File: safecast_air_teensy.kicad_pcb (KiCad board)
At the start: 2 copper layers, 108 x 69.8 mm, 22 parts, among them P1 CONN_5X2, P2 CONN_5X2, P3 CONN_7X2, P4 CONN_2X2, P5 CONN_2, P6 CONN_2, P7 CONN_2, P8 CONN_3X2, P9 CONN_2, U1 GPS, U2 XBEE, U3 LCD, U4 OPENLOG, U5 POLOLU_3V3, U6 TEENSY3.1, U7 R5_BUSSED

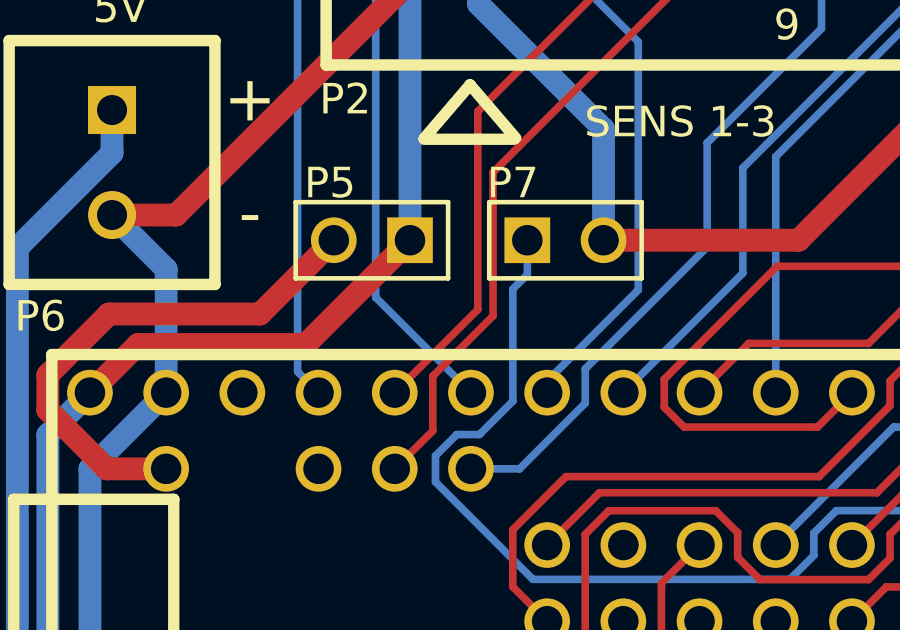
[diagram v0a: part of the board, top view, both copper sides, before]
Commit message: Added missing silkscreen elements (5V VBUS) and PROG.
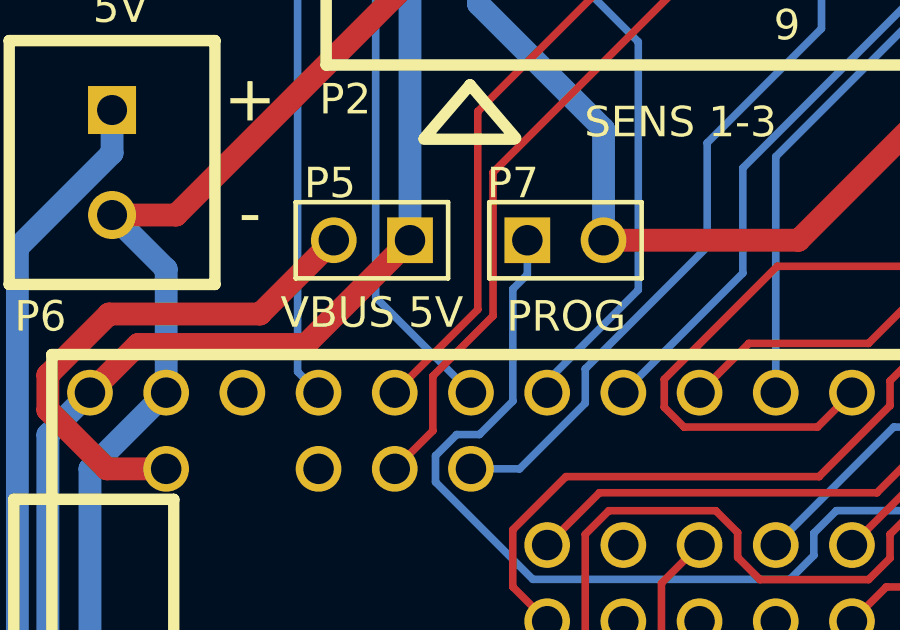
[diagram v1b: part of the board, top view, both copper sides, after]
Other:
- board text added: "PROG"
- board text added: "VBUS 5V"
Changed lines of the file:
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@@
     (area 25.349999 25.349999 133.400001 95.3516)
     (thickness 1.6)
-    (drawings 22)
+    (drawings 24)
     (tracks 409)
     (zones 0)
@@
     (uvia_min_size 0.508)
     (uvia_min_drill 0.127)
-    (pcb_text_width 0.3048)
-    (pcb_text_size 1.524 1.524)
+    (pcb_text_width 0.2032)
+    (pcb_text_size 1.016 1.016)
     (mod_edge_width 0.15)
     (mod_text_size 1 1)
@@
     (visible_elements FFFFFFBF)
     (pcbplotparams
-      (layerselection 3178497)
+      (layerselection 284196865)
       (usegerberextensions true)
       (excludeedgelayer true)
@@
       (outputformat 1)
       (mirror false)
-      (drillshape 1)
+      (drillshape 0)
       (scaleselection 1)
-      (outputdirectory ""))
+      (outputdirectory gerber_v0p1_r1/))
   )
   (net 0 "")
@@
     )
   )
+  (gr_text PROG (at 44.831 44.958) (layer F.SilkS)
+    (effects (font (size 1.016 1.016) (thickness 0.2032)))
+  )
+  (gr_text "VBUS 5V" (at 38.354 44.831) (layer F.SilkS)
+    (effects (font (size 1.016 1.016) (thickness 0.2032)))
+  )
   (gr_text "Safecast Air Prototype V0.1 R1\nwww.iorodeo.com" (at 82.804 61.341 180) (layer B.SilkS)

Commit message: Finished first version of Revision 2.
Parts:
- added R1: R, R_SMALL, F.Cu at (38.0, 41.0)
- added R10: R, R_SMALL, F.Cu at (65.0, 41.0)
- added R11: R, R_SMALL, F.Cu at (68.0, 41.0)
- added R12: R, R_SMALL, F.Cu at (72.0, 38.0)
- added R13: R, R_SMALL, F.Cu at (75.0, 38.0)
- added R14: R, R_SMALL, F.Cu at (78.0, 38.0)
- added R15: R, R_SMALL, F.Cu at (81.0, 38.0)
- added R16: R, R_SMALL, F.Cu at (84.0, 38.0)
- added R17: R, R_SMALL, F.Cu at (87.0, 38.0)
- added R18: R, R_SMALL, F.Cu at (90.0, 38.0)
- added R19: R, R_SMALL, F.Cu at (72.0, 48.0)
- added R2: R, R_SMALL, F.Cu at (41.0, 41.0)
- added R20: R, R_SMALL, F.Cu at (75.0, 48.0)
- added R21: R, R_SMALL, F.Cu at (78.0, 48.0)
- added R22: R, R_SMALL, F.Cu at (81.0, 48.0)
- added R23: R, R_SMALL, F.Cu at (84.0, 48.0)
- added R24: R, R_SMALL, F.Cu at (87.0, 48.0)
- added R3: R, R_SMALL, F.Cu at (44.0, 41.0)
- added R4: R, R_SMALL, F.Cu at (47.0, 41.0)
- added R5: R, R_SMALL, F.Cu at (50.0, 41.0)
- added R6: R, R_SMALL, F.Cu at (53.0, 41.0)
- added R7: R, R_SMALL, F.Cu at (56.0, 41.0)
- added R8: R, R_SMALL, F.Cu at (59.0, 41.0)
- added R9: R, R_SMALL, F.Cu at (62.0, 41.0)
- P1, P2: footprint 5X2_SHRD_HEADER -> 5X2_2MM_SHRD_HEADER
- P3: value CONN_7X2 -> CONN_5X2; footprint 7X2_SHRD_HEADER -> 5X2_SHRD_HEADER
- P8: value CONN_3X2 -> CONN_2; footprint 3X2_SHRD_HEADER -> PIN_ARRAY_2X1
- moved P8 76.8 mm to (38.1, 90.4), turned to 270 degrees
- moved U4 69.3 mm to (45.0, 76.6), turned to 270 degrees
- moved P7 50.0 mm to (58.9, 90.4), turned to 270 degrees
- moved U5 34.2 mm to (56.0, 70.2), turned to 0 degrees
- moved U2 29.3 mm to (81.0, 81.0)
- moved P4 27.1 mm to (45.2, 90.4)
- moved P1 22.3 mm to (46.4, 30.5)
- moved P9 22.0 mm to (52.8, 90.4)
- moved S2 18.2 mm to (30.6, 57.9)
- moved U1 17.6 mm to (80.6, 60.7), turned to 0 degrees
- moved U7 16.1 mm to (112.0, 80.0)
- moved S1 15.5 mm to (112.0, 89.0)
- moved P2 13.3 mm to (60.2, 30.5)
- moved P5 12.0 mm to (37.5, 30.5), turned to 270 degrees
- moved U6 1.40 mm to (45.6, 56.5)
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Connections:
- P1 pad 1: GND -> /5V
- P1 pad 10: (no net) -> GND
- P1 pad 2: /5V -> GND
- P1 pad 3: /OP1_A -> /AUX3
- P1 pad 4: /OP2_A -> /WRK3
- P1 pad 5: /OP1_B -> /AUX2
- P1 pad 6: /OP2_B -> /WRK2
- P1 pad 7: /OP1_C -> /AUX1
- P1 pad 8: /OP2_C -> /WRK1
- P1 pad 9: (no net) -> /TMP1
- P2 pad 1: GND -> /5V
- P2 pad 10: (no net) -> GND
- P2 pad 2: /5V -> GND
- P2 pad 3: /OP1_D -> /AUX6
- P2 pad 4: /OP2_D -> /WRK6
- P2 pad 5: /OP1_E -> /AUX5
- P2 pad 6: /OP2_E -> /WRK5
- P2 pad 7: /OP1_F -> /AUX4
- P2 pad 8: /OP2_F -> /WRK4
- P2 pad 9: (no net) -> /TMP2
- P3 pad 1: GND -> /3V3
- P3 pad 10: /D33 -> /D31
- P3 pad 2: /5V -> GND
- P3 pad 3: /3V3 -> /D32
- P3 pad 4: /SCK -> /D33
- P3 pad 5: /A12 -> /SCL
- P3 pad 6: /MISO -> /SDA
- P3 pad 7: /A13 -> /MISO
- P3 pad 9: /A14,DAC -> /SCK
- P8 pad 1: /D30 -> /A14,DAC
- P8 pad 2: /D29 -> GND
- U3 pad 4: /LCD_CS -> /LCD_RST
- U3 pad 5: (no net) -> /LCD_CS
- U3 pad 6: /5V -> (no net)
- U3 pad 7: (no net) -> /5V
- U6 pad 21: /OP1_A -> /WRK1_DIV
- U6 pad 22: /OP2_A -> /AUX1_DIV
- U6 pad 23: /OP1_B -> /WRK2_DIV
- U6 pad 24: /OP2_B -> /AUX2_DIV
- U6 pad 25: /OP1_C -> /WRK3_DIV
- U6 pad 26: /OP2_C -> /AUX3_DIV
- U6 pad 27: /OP1_D -> /WRK4_DIV
- U6 pad 28: /OP2_D -> /AUX4_DIV
- U6 pad 29: /OP1_E -> /WRK5_DIV
- U6 pad 30: /OP2_E -> /AUX5_DIV
- U6 pad 34: /A12 -> /TMP2
- U6 pad 41: /D29 -> /SCL
- U6 pad 42: /D30 -> /SDA
- U6 pad 47: /A13 -> /TMP1
- U6 pad 48: /OP2_F -> /AUX6_DIV
- U6 pad 49: /OP1_F -> /WRK6_DIV
- U6 pad 6: (no net) -> /LCD_RST
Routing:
- net GND: track 273.2 -> 386.9 mm
- net /LCD_RST: track 0.00 -> 94.4 mm
- net /SDA: track 0.00 -> 81.7 mm
- net /5V: track 264.6 -> 187.8 mm
- net /D30: track 76.2 -> 0.00 mm, vias 1 -> 0
- net /A12: track 75.8 -> 0.00 mm
- net /A13: track 73.8 -> 0.00 mm
- net /D29: track 72.4 -> 0.00 mm, vias 2 -> 0
- net /LOG_GRN: track 84.5 -> 20.5 mm
- net /SCL: track 0.00 -> 62.7 mm, vias 0 -> 1
- net /TMP2: track 0.00 -> 60.9 mm
- net /LOG_TXO: track 76.4 -> 15.7 mm
- net /WRK5_DIV: track 0.00 -> 59.6 mm
- net /LOG_RXI: track 77.5 -> 19.1 mm
- net /AUX4_DIV: track 0.00 -> 55.4 mm, vias 0 -> 1
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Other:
- board text added: "3V3SEL"
- board text added: "3V3SHD"
- board text added: "AOUT"
- board text added: "Safecast Air Prototype V0.1 R2 www.iorodeo.com"
- board text added: "TNY"
- board text added: "UEXT"
- board text added: "VBUS"
- board text removed: "3V3 SEL"
- board text removed: "3V3 SHDN"
- board text removed: "EXPANSION"
- board text removed: "SENS T/H"
- board text removed: "Safecast Air Prototype V0.1 R1 www.iorodeo.com"
- board text removed: "TNSY"
- board text removed: "VBUS 5V"

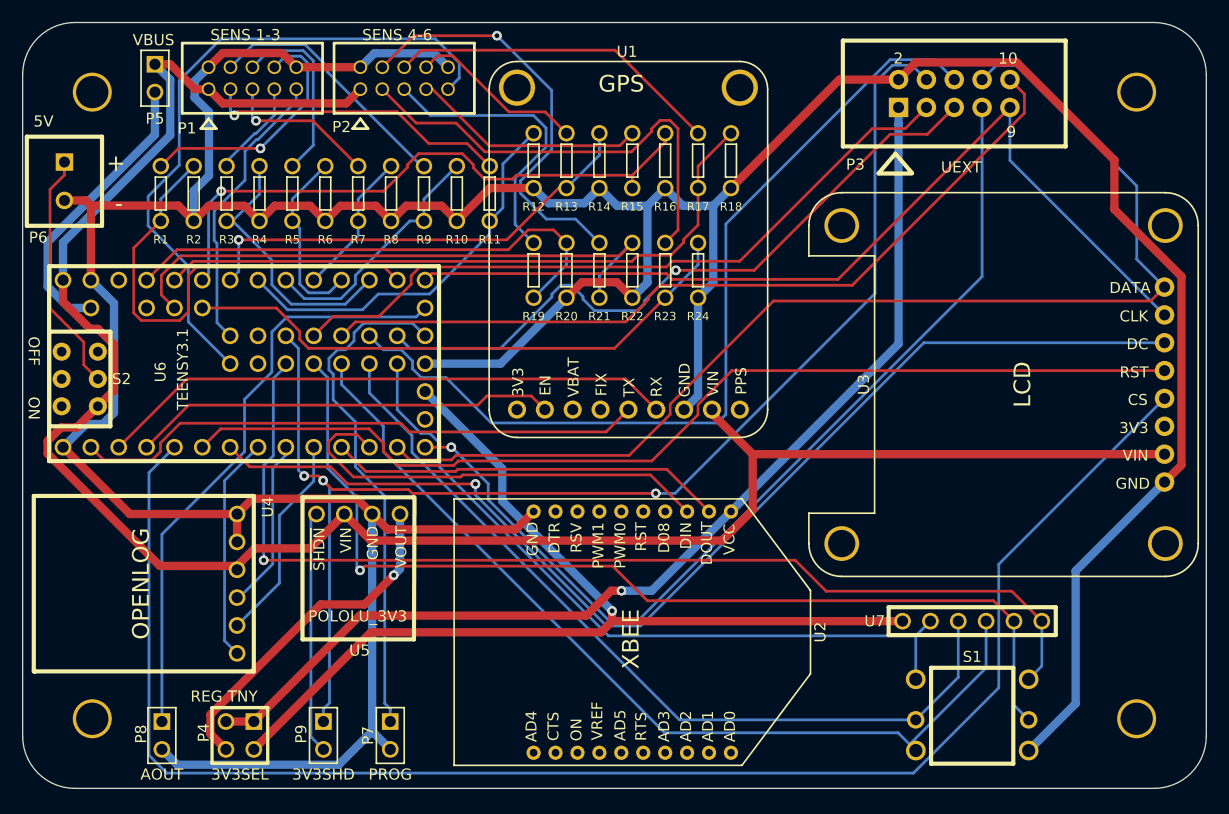
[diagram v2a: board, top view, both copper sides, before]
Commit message: Moved GPS slightly. Re-routed board.
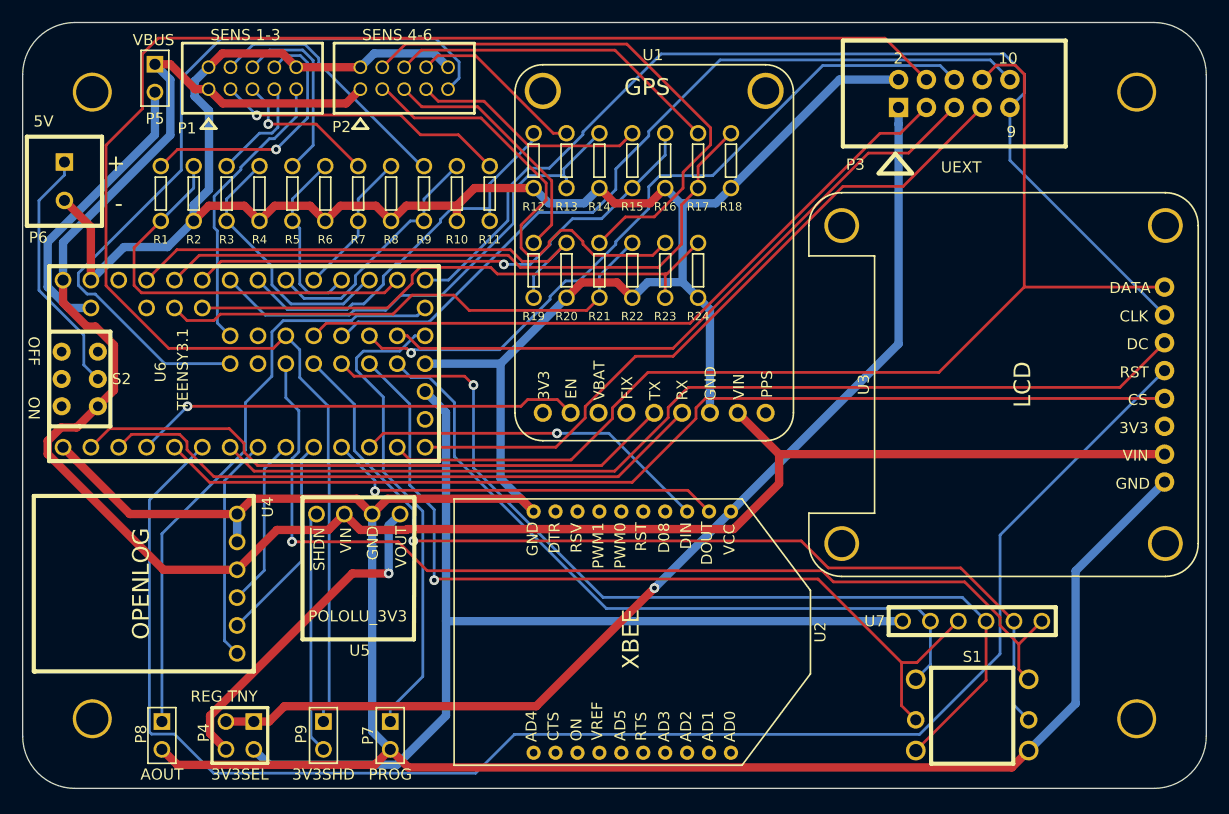
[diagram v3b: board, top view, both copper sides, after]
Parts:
- moved U1 2.37 mm to (83.0, 61.0)
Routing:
- net /LCD_RST: track 94.4 -> 143.7 mm
- net /LCD_CS: track 143.1 -> 95.4 mm
- net /D33: track 121.3 -> 152.4 mm, vias 3 -> 0
- net /MISO: track 86.6 -> 64.2 mm, vias 1 -> 0
- net /SDA: track 81.7 -> 66.8 mm, vias 0 -> 1
- net /WRK6: track 38.3 -> 50.2 mm, vias 1 -> 0
- net /LCD_DC: track 103.3 -> 91.5 mm, vias 1 -> 0
- net /TMP2: track 60.9 -> 70.2 mm
- net /SCK: track 85.1 -> 94.2 mm
- net /XBEE_DIN: track 40.5 -> 32.5 mm, vias 0 -> 1
- net /WRK1_DIV: track 44.4 -> 37.9 mm
- net /WRK6_DIV: track 53.9 -> 47.5 mm
- net /AUX4_DIV: track 55.4 -> 49.4 mm
- net /MOSI: track 107.0 -> 101.7 mm
- net /JOY_D: track 92.0 -> 87.3 mm
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
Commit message: Added gerber files for version 0.1 revision 2.
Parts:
- moved P2 2.04 mm to (62.2, 30.6)
- moved P1 1.78 mm to (48.1, 30.6)
- moved P5 0.25 mm to (37.7, 30.5)
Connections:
- P9 pad 1: /D33 -> /D31
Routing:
- net /D33: track 152.4 -> 70.1 mm
- net /LCD_RST: track 143.7 -> 94.2 mm
- net /AUX1: track 9.76 -> 48.6 mm
- net /D31: track 73.5 -> 111.3 mm, vias 0 -> 1
- net /JOY_CENT: track 94.1 -> 120.9 mm, vias 1 -> 0
- net /TMP1: track 26.5 -> 46.1 mm
- net /TMP2: track 70.2 -> 52.4 mm
- net /AUX4_DIV: track 49.4 -> 61.0 mm, vias 1 -> 0
- net /3V3_TNSY: track 92.0 -> 102.0 mm
- net /WRK4_DIV: track 45.2 -> 51.2 mm
- net /MOSI: track 101.7 -> 107.4 mm
- net /WRK3: track 23.4 -> 28.2 mm
- net /AUX6: track 41.5 -> 37.5 mm, vias 0 -> 1
- net /WRK1_DIV: track 37.9 -> 34.2 mm
- net /D32: track 64.5 -> 68.0 mm
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
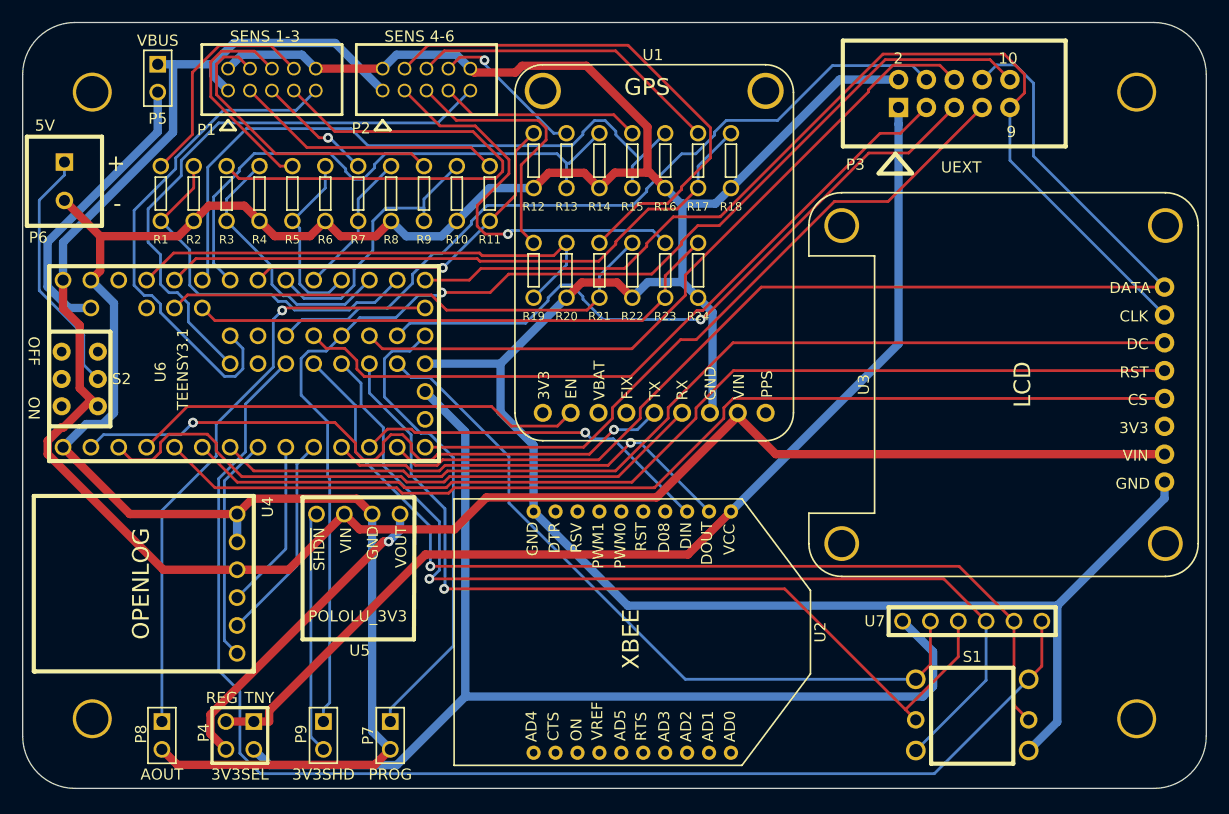
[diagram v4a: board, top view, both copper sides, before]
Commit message: Added header for PM 2.5 & PM 10 sensor.  Adjusted silkscreen and spacing on gas sensor headers - to get rid on collision issue when using to gas sensor cables simultaneously.  Rerouted board.
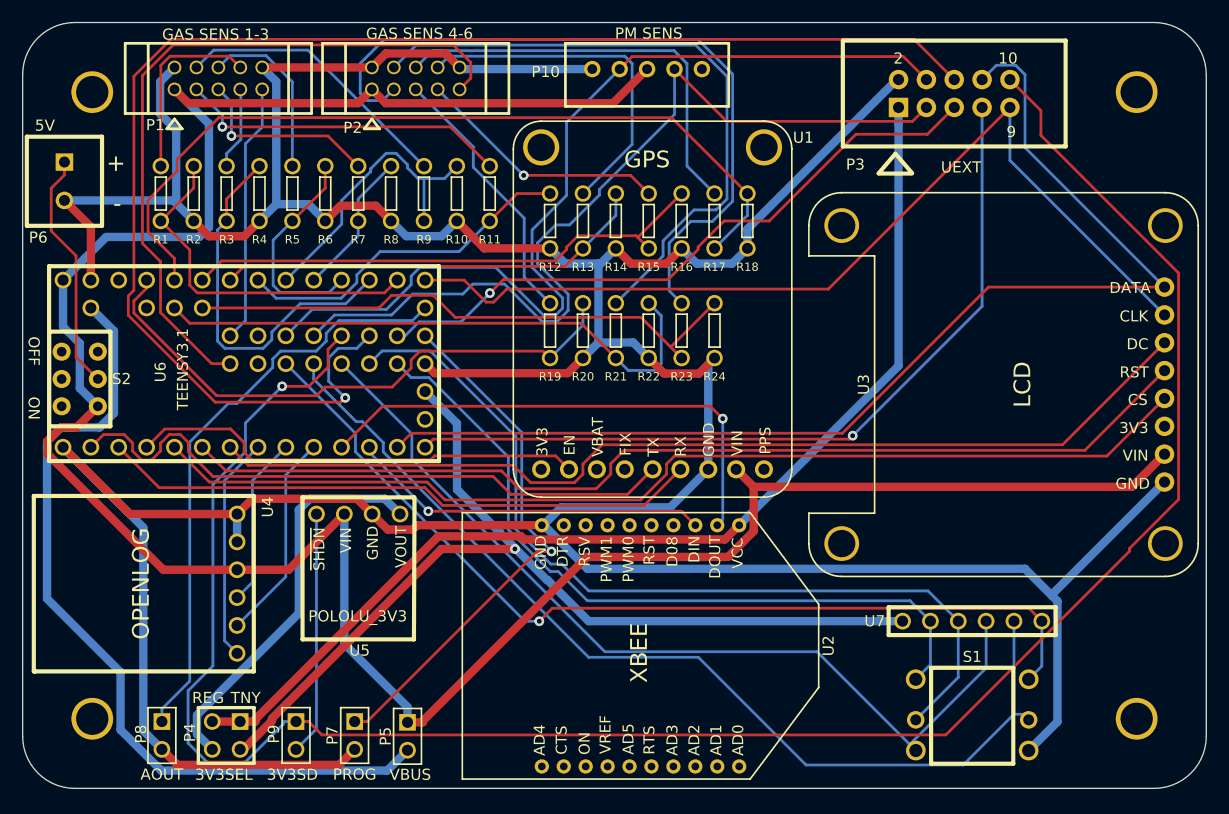
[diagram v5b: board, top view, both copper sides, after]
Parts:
- added P10: CONN_5_MOD, JST_XH_5PIN, F.Cu at (82.3, 29.6)
- moved P5 64.2 mm to (60.5, 90.5)
- moved R12 5.70 mm to (73.5, 43.5)
- moved R13 5.70 mm to (76.5, 43.5)
- moved R14 5.70 mm to (79.5, 43.5)
- moved R15 5.70 mm to (82.5, 43.5)
- moved R16 5.70 mm to (85.5, 43.5)
- moved R17 5.70 mm to (88.5, 43.5)
- moved R18 5.70 mm to (91.5, 43.5)
- moved R19 5.70 mm to (73.5, 53.5)
- moved R20 5.70 mm to (76.5, 53.5)
- moved R21 5.70 mm to (79.5, 53.5)
- moved R22 5.70 mm to (82.5, 53.5)
- moved R23 5.70 mm to (85.5, 53.5)
- moved R24 5.70 mm to (88.5, 53.5)
- moved U1 5.15 mm to (82.8, 66.2)
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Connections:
- net /D32 renamed /PWM1
- net /D33 renamed /PWM2
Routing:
- net /D31: track 111.3 -> 191.3 mm
- net /SDA: track 66.3 -> 131.8 mm, vias 0 -> 1
- net /5V: track 184.4 -> 233.8 mm
- net /VBUS: track 26.7 -> 75.2 mm
- net /AUX1: track 48.6 -> 7.56 mm
- net /JOY_CENT: track 120.9 -> 86.4 mm, vias 0 -> 1
- net /AUX6: track 37.5 -> 67.6 mm, vias 1 -> 0
- net /TMP1: track 46.1 -> 23.7 mm
- net GND: track 384.2 -> 403.6 mm
- net /WRK5_DIV: track 57.8 -> 75.8 mm
- net /WRK4: track 14.3 -> 32.1 mm, vias 1 -> 0
- net /PWM2: track 70.1 -> 86.0 mm
- net /PWM1: track 68.0 -> 81.5 mm
- net /3V3_TNSY: track 102.0 -> 88.6 mm, vias 0 -> 1
- net /TMP2: track 52.4 -> 65.2 mm
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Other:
- board text added: "3V3SD"
- board text added: "GAS SENS 1-3"
- board text added: "GAS SENS 4-6"
- board text added: "PM SENS"
- board text added: "Safecast Air Prototype V0.1 R3 www.iorodeo.com"
- board text removed: "3V3SHD"
- board text removed: "SENS 1-3"
- board text removed: "SENS 4-6"
- board text removed: "Safecast Air Prototype V0.1 R2 www.iorodeo.com"
